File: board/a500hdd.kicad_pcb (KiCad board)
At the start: 2 copper layers, 46.8 x 111 mm, 108 parts, among them J1 Conn_01x04_Male, U1 ata_connector, U2 ata_connector44, U3 74LS04, U4 a500exp, U5 74LS00, U6 74LS08, U7 74LS08, U8 a500exp, U9 a500exp

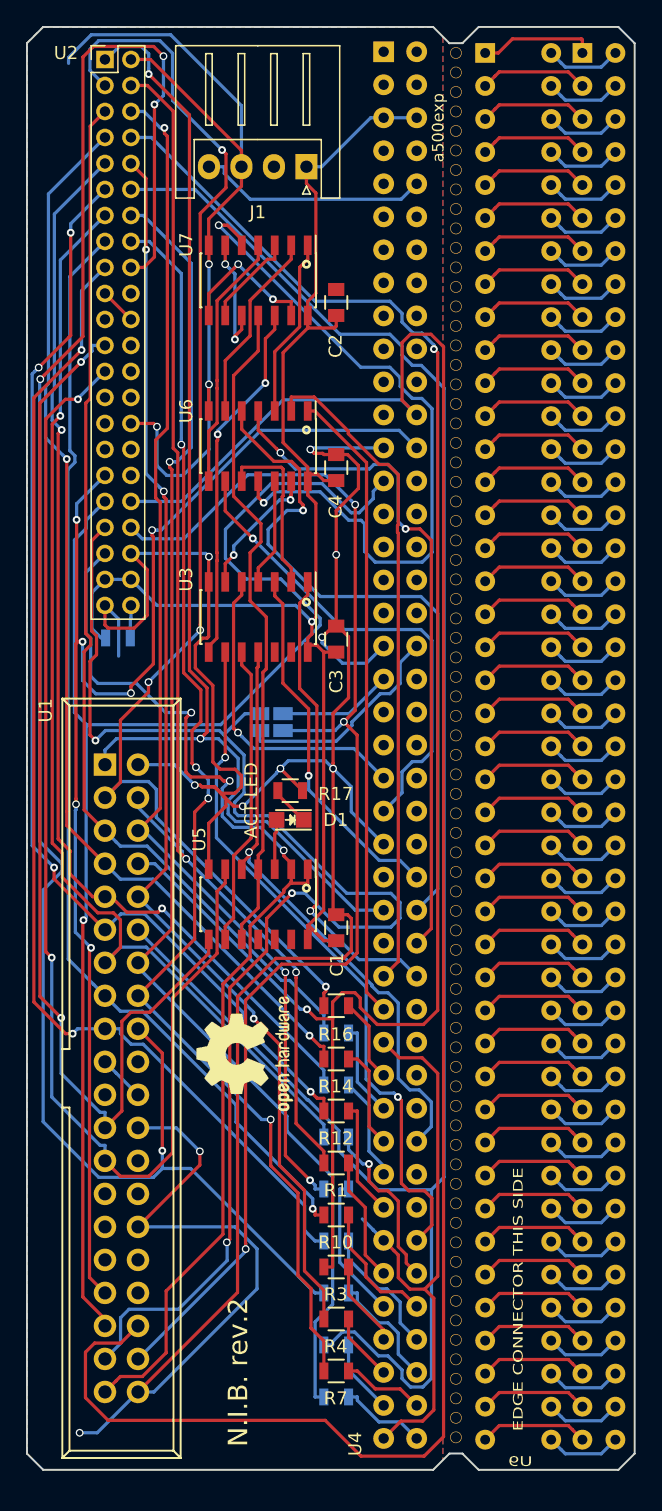
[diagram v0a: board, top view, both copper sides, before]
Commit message: changed drills on board break line from PTH to NPTH
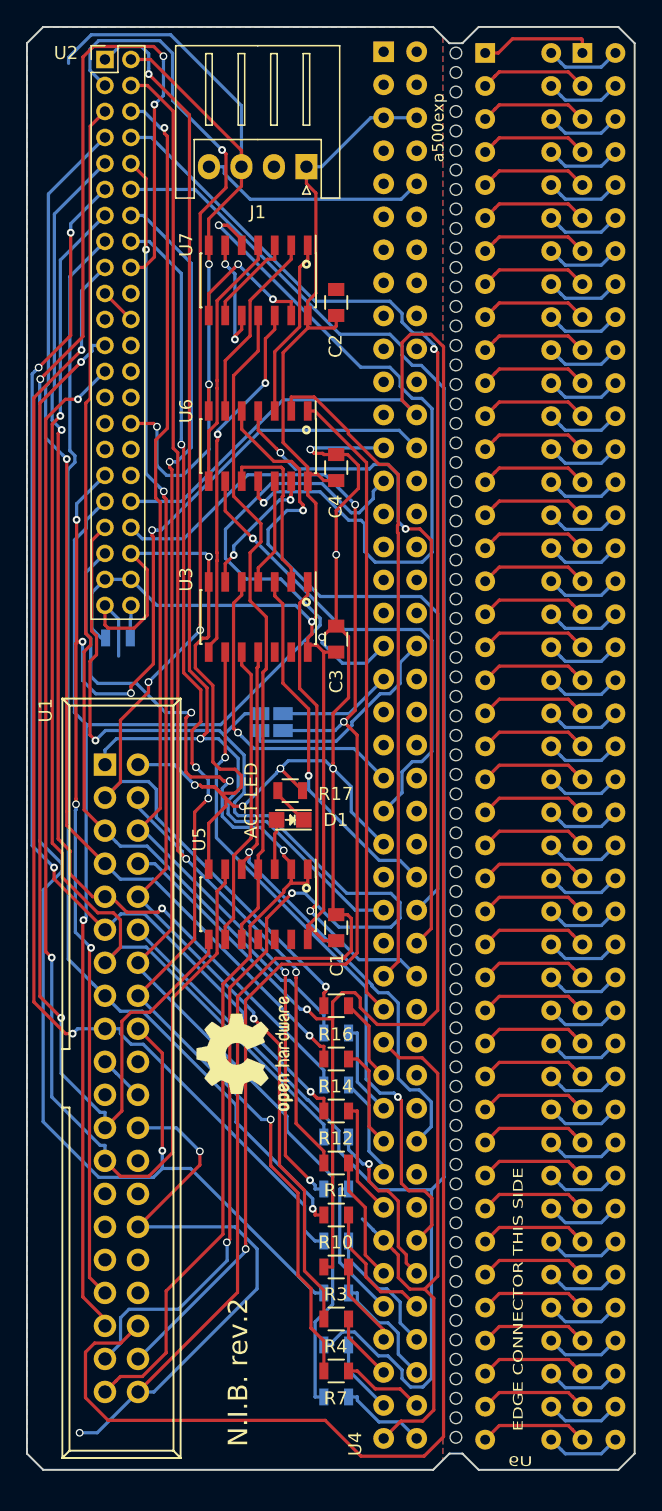
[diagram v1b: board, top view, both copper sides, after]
